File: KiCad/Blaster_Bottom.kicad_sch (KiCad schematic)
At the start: 22 parts, among them Q1 BUK9832-55A, Q2 BUK9832-55A, Q3 BUK9832-55A, U2 PIC16F1788-IP

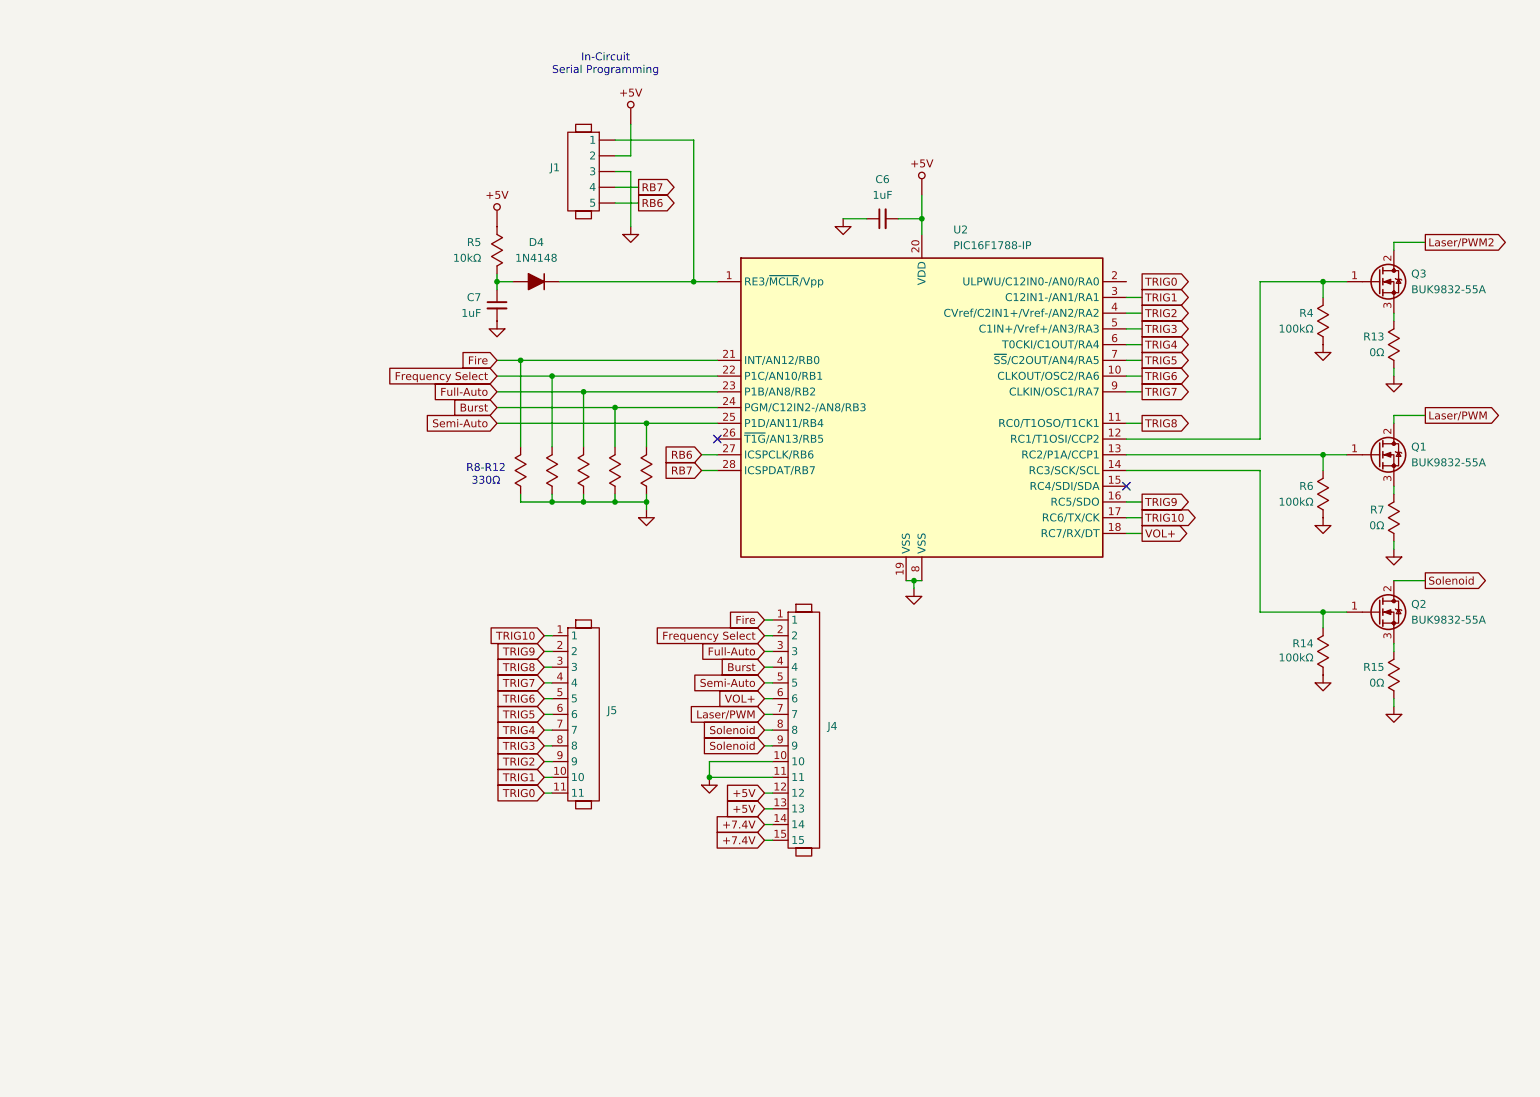
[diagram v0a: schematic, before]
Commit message: fixed the schematics, and got the new components added into the PCB, need to rerun a lot of traces.
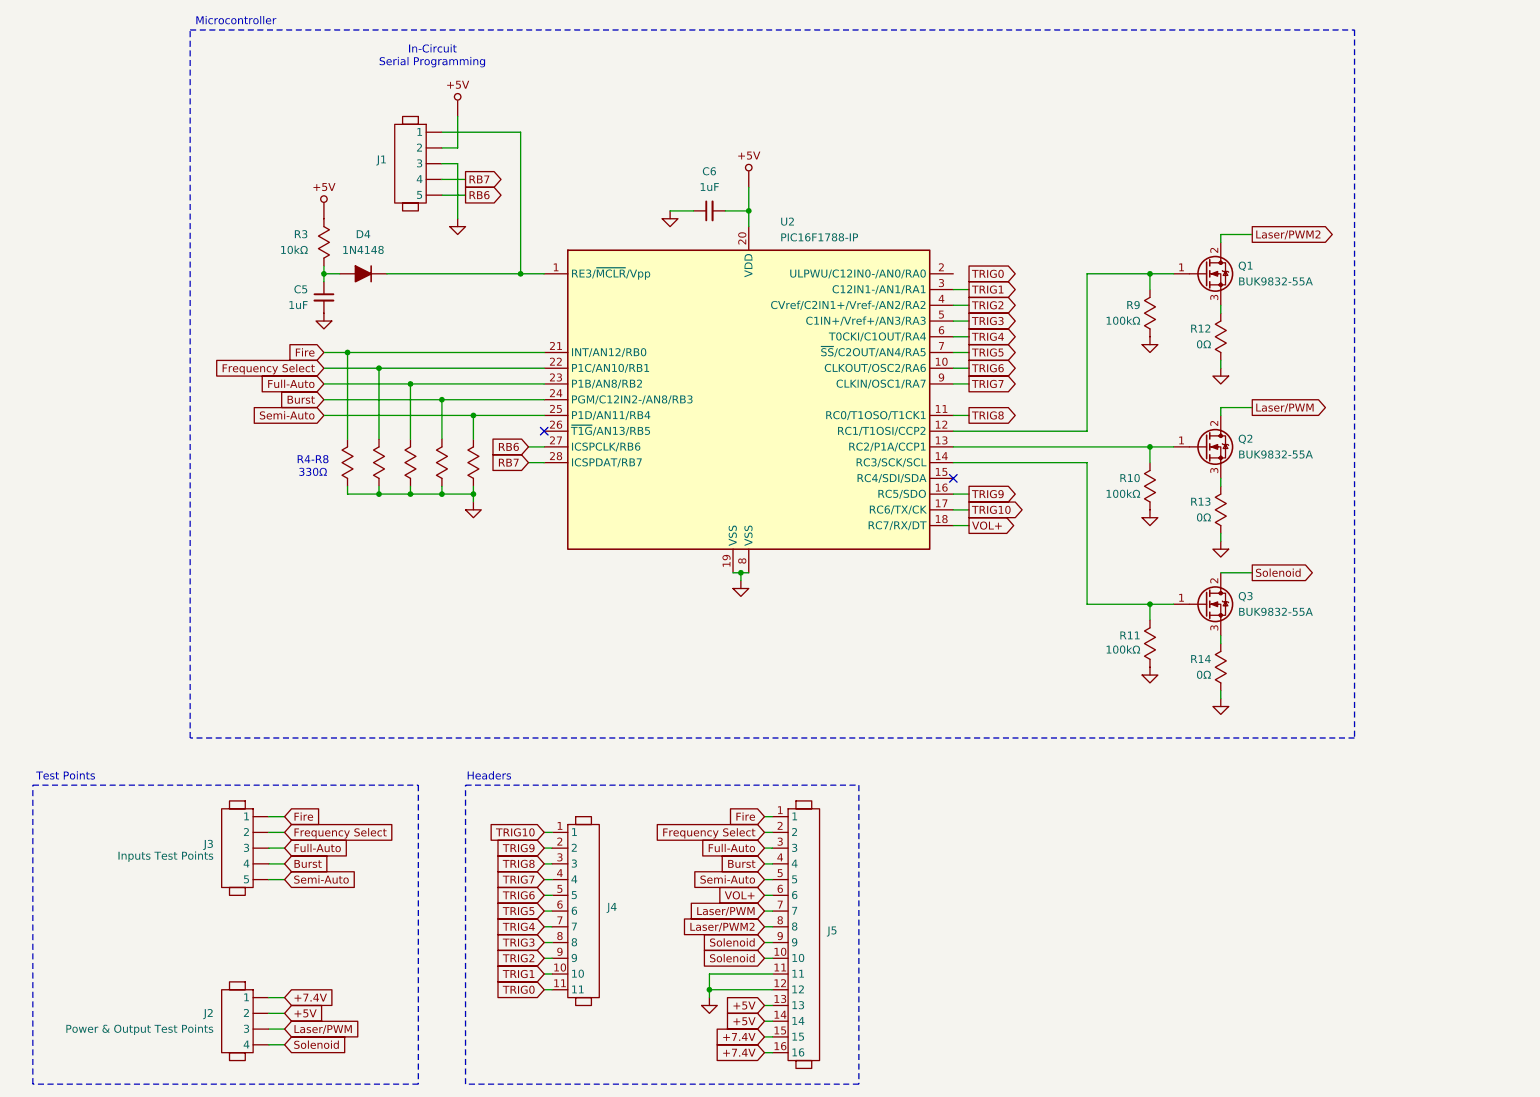
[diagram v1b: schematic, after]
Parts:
- added J2: Power & Output Test Points, Connector_PinHeader_2.54mm:PinHeader_1x04_P2.54mm_Vertical, symbol Libraries:Header_1x4
- added J3: Inputs Test Points, Connector_PinHeader_2.54mm:PinHeader_1x05_P2.54mm_Vertical, symbol Libraries:Header_1x5
- J4: renamed from J5; footprint (none) -> Connector_PinHeader_2.54mm:PinHeader_1x11_P2.54mm_Vertical
- J5: renamed from J4; footprint (none) -> Connector_PinHeader_2.54mm:PinHeader_1x16_P2.54mm_Vertical; symbol Libraries:Header_1x15 -> Libraries:Header_1x16
- renumbered C7 to C5, Q3 to Q1, Q1 to Q2, Q2 to Q3, R6 to R10, R14 to R11, R13 to R12, R7 to R13, R15 to R14, R5 to R3, R8 to R4, R9 to R5, R10 to R6, R11 to R7, R12 to R8, R4 to R9
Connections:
- net +5V: now also J5.14, J2.2; no longer J5.12
- net +7.4V: now also J5.16, J2.1; no longer J5.14
- net Burst: now also J3.4
- net Fire: now also J3.1
- net Frequency Select: now also J3.2
- net Full-Auto: now also J3.3
- net Laser/PWM: now also J2.3
- net Laser/PWM2: now also J5.8
- net Semi-Auto: now also J3.5
- net Solenoid: now also J5.10, J2.4; no longer J5.8
- net at J5.11: now also J5.12; no longer J5.10
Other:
- note added: "Headers"
- note added: "Microcontroller"
- note added: "R4-R8 330Ω"
- note added: "Test Points"
- note removed: "R8-R12 330Ω"
- moved on the sheet: C5, C6, D4, J1, J4, Q1, Q2, Q3, R10, R11, R12, R13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

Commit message: PCB nearly done for the blaster
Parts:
- J2: footprint Connector_PinHeader_2.54mm:PinHeader_1x04_P2.54mm_Vertical -> Connector_PinHeader_2.54mm:PinHeader_1x05_P2.54mm_Vertical; symbol Libraries:Header_1x4 -> Libraries:Header_1x5
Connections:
- net Laser/PWM: now also J2.5; no longer J2.3
- net Laser/PWM2: now also J2.4
- net Solenoid: now also J2.3; no longer J2.4

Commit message: finished blaster PCB
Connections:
- net TRIG0: now also U2.2 (ULPWU/C12IN0-/AN0/RA0)
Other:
- moved on the sheet: J2, J3
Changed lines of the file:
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@@
 	(title_block
 		(title "Blaster Bottom")
-		(date "2025-04-18")
+		(date "2025-04-21")
 		(rev "A")
 		(company "Idaho State University")
@@
 	(wire
 		(pts
-			(xy 60.96 162.56) (xy 58.42 162.56)
+			(xy 60.96 165.1) (xy 58.42 165.1)
 		)
 		(stroke
@@
 	(wire
 		(pts
+			(xy 168.91 67.31) (xy 171.45 67.31)
+		)
+		(stroke
+			(width 0)
+			(type default)
+		)
+	)
+	(wire
+		(pts
 			(xy 217.17 88.9) (xy 212.09 88.9)
 		)
@@
 	(wire
 		(pts
-			(xy 60.96 154.94) (xy 58.42 154.94)
+			(xy 60.96 157.48) (xy 58.42 157.48)
 		)
 		(stroke
@@
 	(wire
 		(pts
-			(xy 58.42 191.77) (xy 60.96 191.77)
+			(xy 58.42 187.96) (xy 60.96 187.96)
 		)
 		(stroke
@@
 	(wire
 		(pts
-			(xy 60.96 157.48) (xy 58.42 157.48)
+			(xy 60.96 160.02) (xy 58.42 160.02)
 		)
 		(stroke
@@
 	(wire
 		(pts
-			(xy 60.96 165.1) (xy 58.42 165.1)
+			(xy 60.96 167.64) (xy 58.42 167.64)
 		)
 		(stroke
@@
 	(wire
 		(pts
-			(xy 58.42 189.23) (xy 60.96 189.23)
+			(xy 58.42 185.42) (xy 60.96 185.42)
 		)
 		(stroke
@@
 	(wire
 		(pts
-			(xy 58.42 194.31) (xy 60.96 194.31)
+			(xy 58.42 190.5) (xy 60.96 190.5)
 		)
 		(stroke
@@
 	(wire
 		(pts
-			(xy 58.42 186.69) (xy 60.96 186.69)
+			(xy 58.42 182.88) (xy 60.96 182.88)
 		)
 		(stroke
@@
 	(wire
 		(pts
-			(xy 58.42 184.15) (xy 60.96 184.15)
+			(xy 58.42 180.34) (xy 60.96 180.34)
 		)
 		(stroke
@@
 	(wire
 		(pts
-			(xy 60.96 160.02) (xy 58.42 160.02)
+			(xy 60.96 162.56) (xy 58.42 162.56)
 		)
 		(stroke
@@
 	(global_label "Laser{slash}PWM2"
 		(shape input)
-		(at 60.96 191.77 0)
+		(at 60.96 187.96 0)
 		(fields_autoplaced yes)
 		(effects
@@
 		)
 		(property "Intersheetrefs" "${INTERSHEET_REFS}"
-			(at 75.738 191.77 0)
+			(at 75.738 187.96 0)
 			(effects
 				(font
@@
 	(global_label "Laser{slash}PWM"
 		(shape input)
-		(at 60.96 194.31 0)
+		(at 60.96 190.5 0)
 		(fields_autoplaced yes)
 		(effects
@@
 		)
 		(property "Intersheetrefs" "${INTERSHEET_REFS}"
-			(at 74.5285 194.31 0)
+			(at 74.5285 190.5 0)
 			(effects
 				(font
@@
 	(global_label "Semi-Auto"
 		(shape input)
-		(at 60.96 165.1 0)
+		(at 60.96 167.64 0)
 		(fields_autoplaced yes)
 		(effects
@@
 		)
 		(property "Intersheetrefs" "${INTERSHEET_REFS}"
-			(at 74.2261 165.1 0)
+			(at 74.2261 167.64 0)
 			(effects
 				(font
@@
 	(global_label "Solenoid"
 		(shape input)
-		(at 60.96 189.23 0)
+		(at 60.96 185.42 0)
 		(fields_autoplaced yes)
 		(effects
@@
 		)
 		(property "Intersheetrefs" "${INTERSHEET_REFS}"
-			(at 72.1093 189.23 0)
+			(at 72.1093 185.42 0)
 			(effects
 				(font
@@
 	(global_label "+7.4V"
 		(shape input)
-		(at 60.96 184.15 0)
+		(at 60.96 180.34 0)
 		(fields_autoplaced yes)
 		(effects
@@
 		)
 		(property "Intersheetrefs" "${INTERSHEET_REFS}"
-			(at 69.63 184.15 0)
+			(at 69.63 180.34 0)
 			(effects
 				(font
@@
 	(global_label "Full-Auto"
 		(shape input)
-		(at 60.96 160.02 0)
+		(at 60.96 162.56 0)
 		(fields_autoplaced yes)
 		(effects
@@
 		)
 		(property "Intersheetrefs" "${INTERSHEET_REFS}"
-			(at 73.1979 160.02 0)
+			(at 73.1979 162.56 0)
 			(effects
 				(font
@@
 	(global_label "Burst"
 		(shape input)
-		(at 60.96 162.56 0)
+		(at 60.96 165.1 0)
 		(fields_autoplaced yes)
 		(effects
@@
 		)
 		(property "Intersheetrefs" "${INTERSHEET_REFS}"
-			(at 68.9042 162.56 0)
+			(at 68.9042 165.1 0)
 			(effects
 				(font
@@
 	(global_label "Fire"
 		(shape input)
-		(at 60.96 154.94 0)
+		(at 60.96 157.48 0)
 		(fields_autoplaced yes)
 		(effects
@@
 		)
 		(property "Intersheetrefs" "${INTERSHEET_REFS}"
-			(at 67.5134 154.94 0)
+			(at 67.5134 157.48 0)
 			(effects
 				(font
@@
 	(global_label "+5V"
 		(shape input)
-		(at 60.96 186.69 0)
+		(at 60.96 182.88 0)
 		(fields_autoplaced yes)
 		(effects
@@
 		)
 		(property "Intersheetrefs" "${INTERSHEET_REFS}"
-			(at 67.8157 186.69 0)
+			(at 67.8157 182.88 0)
 			(effects
 				(font
@@
 	(global_label "Frequency Select"
 		(shape input)
-		(at 60.96 157.48 0)
+		(at 60.96 160.02 0)
 		(fields_autoplaced yes)
 		(effects
@@
 		)
 		(property "Intersheetrefs" "${INTERSHEET_REFS}"
-			(at 80.3342 157.48 0)
+			(at 80.3342 160.02 0)
 			(effects
 				(font
@@
 	(symbol
 		(lib_id "Libraries:Header_1x5")
-		(at 53.34 180.34 0)
+		(at 53.34 176.53 0)
 		(mirror y)
 		(unit 1)
@@
 		(dnp no)
 		(property "Reference" "J2"
-			(at 50.038 187.96 0)
+			(at 50.038 184.15 0)
 			(effects
 				(font
@@
 		)
 		(property "Value" "Power & Output Test Points"
-			(at 50.038 190.5 0)
+			(at 50.038 186.69 0)
 			(effects
 				(font
@@
 		)
 		(property "Footprint" "Connector_PinHeader_2.54mm:PinHeader_1x05_P2.54mm_Vertical"
-			(at 53.34 180.34 0)
+			(at 53.34 176.53 0)
 			(effects
 				(font
@@
 		)
 		(property "Datasheet" ""
-			(at 53.34 180.34 0)
+			(at 53.34 176.53 0)
 			(effects
 				(font
@@
 		)
 		(property "Description" ""
-			(at 53.34 180.34 0)
+			(at 53.34 176.53 0)
 			(effects
 				(font
@@
 	(symbol
 		(lib_id "Libraries:Header_1x5")
-		(at 53.34 151.13 0)
+		(at 53.34 153.67 0)
 		(mirror y)
 		(unit 1)
@@
 		(dnp no)
 		(property "Reference" "J3"
-			(at 49.53 159.3849 0)
+			(at 49.53 161.9249 0)
 			(effects
 				(font
@@
 		)
 		(property "Value" "Inputs Test Points"
-			(at 49.53 161.29 0)
+			(at 49.53 163.83 0)
 			(effects
 				(font
@@
 		)
 		(property "Footprint" "Connector_PinHeader_2.54mm:PinHeader_1x05_P2.54mm_Vertical"
-			(at 53.34 151.13 0)
+			(at 53.34 153.67 0)
 			(effects
 				(font
@@
 		)
 		(property "Datasheet" ""
-			(at 53.34 151.13 0)
+			(at 53.34 153.67 0)
 			(effects
 				(font
@@
 		)
 		(property "Description" ""
-			(at 53.34 151.13 0)
+			(at 53.34 153.67 0)
 			(effects
 				(font

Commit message: updated blaster schematic
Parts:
- R4, R5, R6, R7, R8: value 330Ω -> 1kΩ
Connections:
- net +7.4V renamed +12V
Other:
- note added: "R4-R8 1kΩ"
- note removed: "R4-R8 330Ω"
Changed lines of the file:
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@@
 		)
 	)
-	(text "R4-R8\n330Ω"
+	(text "R4-R8\n1kΩ"
 		(exclude_from_sim no)
 		(at 65.532 98.552 0)
@@
 		)
 	)
-	(global_label "+7.4V"
+	(global_label "+12V"
 		(shape input)
 		(at 60.96 180.34 0)
@@
 		)
 		(property "Intersheetrefs" "${INTERSHEET_REFS}"
-			(at 69.63 180.34 0)
+			(at 69.0252 180.34 0)
 			(effects
 				(font
@@
 		)
 	)
-	(global_label "+7.4V"
+	(global_label "+12V"
 		(shape input)
 		(at 138.43 193.04 180)
@@
 		)
 		(property "Intersheetrefs" "${INTERSHEET_REFS}"
-			(at 129.76 193.04 0)
+			(at 130.3648 193.04 0)
 			(effects
 				(font
@@
 		)
 	)
-	(global_label "+7.4V"
+	(global_label "+12V"
 		(shape input)
 		(at 138.43 190.5 180)
@@
 		)
 		(property "Intersheetrefs" "${INTERSHEET_REFS}"
-			(at 129.76 190.5 0)
+			(at 130.3648 190.5 0)
 			(effects
 				(font
@@
 			)
 		)
-		(property "Value" "330Ω"
+		(property "Value" "1kΩ"
 			(at 80.01 99.06 90)
 			(effects
@@
 			)
 		)
-		(property "Value" "330Ω"
+		(property "Value" "1kΩ"
 			(at 68.58 98.806 90)
 			(effects
@@
 			)
 		)
-		(property "Value" "330Ω"
+		(property "Value" "1kΩ"
 			(at 74.93 99.06 90)
 			(effects
@@
 			)
 		)
-		(property "Value" "330Ω"
+		(property "Value" "1kΩ"
 			(at 85.09 99.06 90)
 			(effects
@@
 			)
 		)
-		(property "Value" "330Ω"
+		(property "Value" "1kΩ"
 			(at 90.17 99.06 90)
 			(effects
